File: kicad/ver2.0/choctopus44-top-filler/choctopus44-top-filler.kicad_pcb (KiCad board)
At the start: 2 copper layers, 247.4 x 118.5 mm, 90 parts, among them SW1 SW_PUSH, SW10 SW_PUSH, SW11 SW_PUSH, SW12 SW_PUSH, SW13 SW_PUSH, SW14 SW_PUSH, SW15 SW_PUSH, SW16 SW_PUSH, SW17 SW_PUSH, SW18 SW_PUSH, SW19 SW_PUSH, SW2 SW_PUSH, SW20 SW_PUSH, SW21 SW_PUSH, SW22 SW_PUSH, SW23 SW_PUSH, SW24 SW_PUSH, SW25 SW_PUSH, SW26 SW_PUSH, SW27 SW_PUSH, SW28 SW_PUSH, SW29 SW_PUSH, SW3 SW_PUSH, SW30 SW_PUSH, SW31 SW_PUSH, SW32 SW_PUSH, SW33 SW_PUSH, SW34 SW_PUSH, SW35 SW_PUSH, SW36 SW_PUSH, SW37 SW_PUSH, SW38 SW_PUSH, SW39 SW_PUSH, SW4 SW_PUSH, SW40 SW_PUSH, SW41 SW_PUSH, SW42 SW_PUSH, SW43 SW_PUSH, SW44 SW_PUSH, SW45 Rotary_Encoder_Switch, SW5 SW_PUSH, SW6 SW_PUSH, SW7 SW_PUSH, SW8 SW_PUSH, SW9 SW_PUSH

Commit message: simplify filler foam files for faster laser cutting
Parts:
- removed D37, D38, D39, D40, D41, D42, D43, D44: 1N4148W, custom-electronics:hybrid-diode-topfoam-cutout
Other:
- outline, holes or cut-outs redrawn

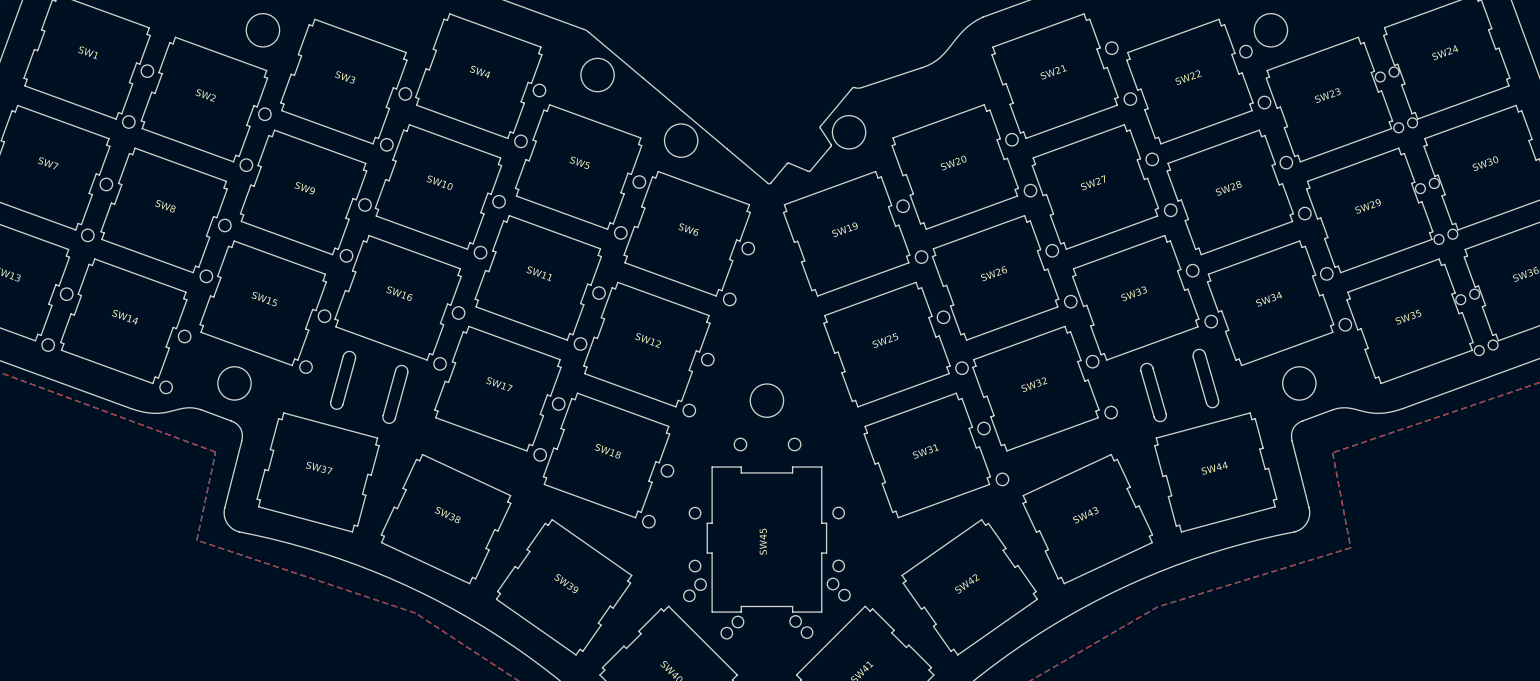
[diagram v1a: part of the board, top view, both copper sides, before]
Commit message: modify foam files to have better cutting tolerances
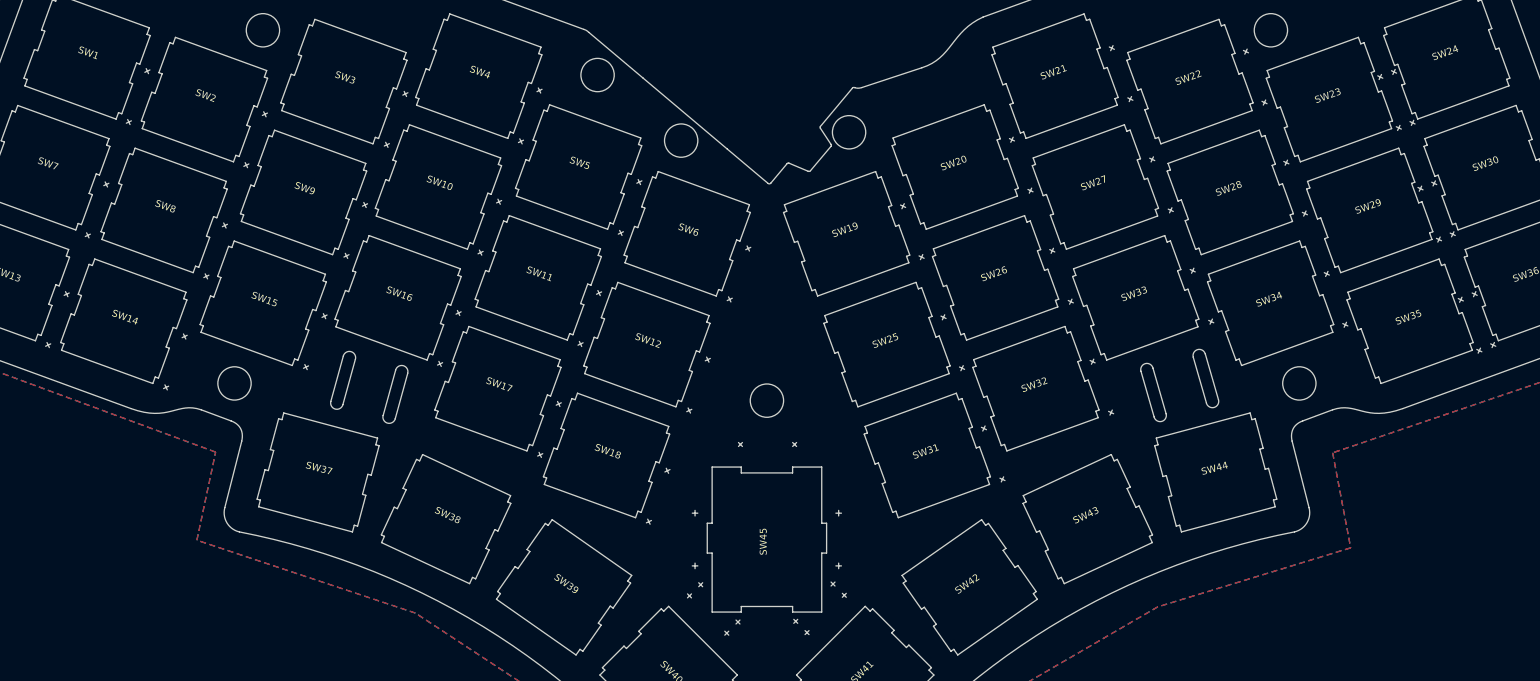
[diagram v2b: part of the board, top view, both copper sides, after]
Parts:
- added D22: 1N4148W, custom-electronics:hybrid-diode-topfoam-cutout, F.Cu at (243.8, 73.5)
- added D22: 1N4148W, custom-electronics:hybrid-diode-topfoam-cutout, F.Cu at (238.0, 57.4)
- added D22: 1N4148W, custom-electronics:hybrid-diode-topfoam-cutout, F.Cu at (249.6, 89.4)
- added D22: 1N4148W, custom-electronics:hybrid-diode-topfoam-cutout, F.Cu at (241.8, 74.2)
- added D22: 1N4148W, custom-electronics:hybrid-diode-topfoam-cutout, F.Cu at (236.0, 58.1)
- added D22: 1N4148W, custom-electronics:hybrid-diode-topfoam-cutout, F.Cu at (247.6, 90.3)
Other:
- outline, holes or cut-outs redrawn

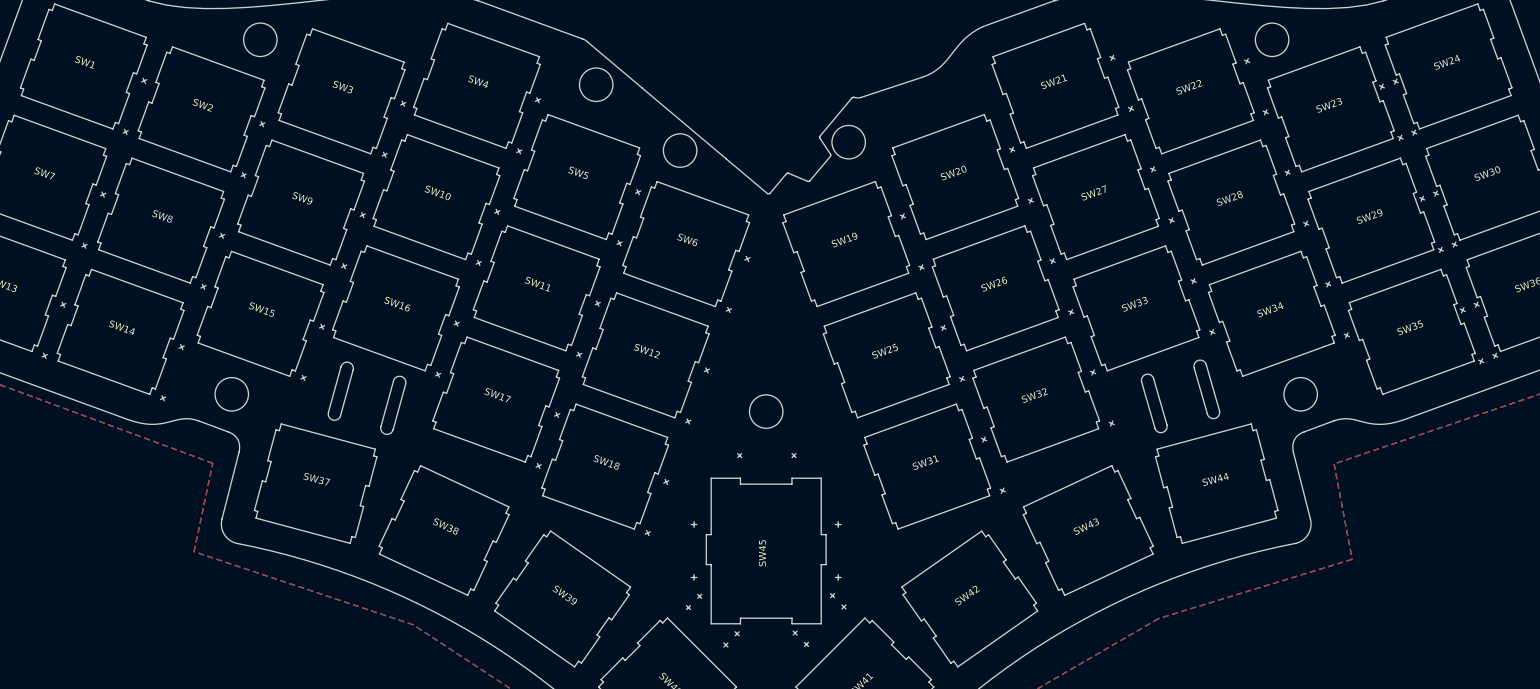
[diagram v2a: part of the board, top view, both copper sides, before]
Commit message: further optimize switch plate foams for laser cutting
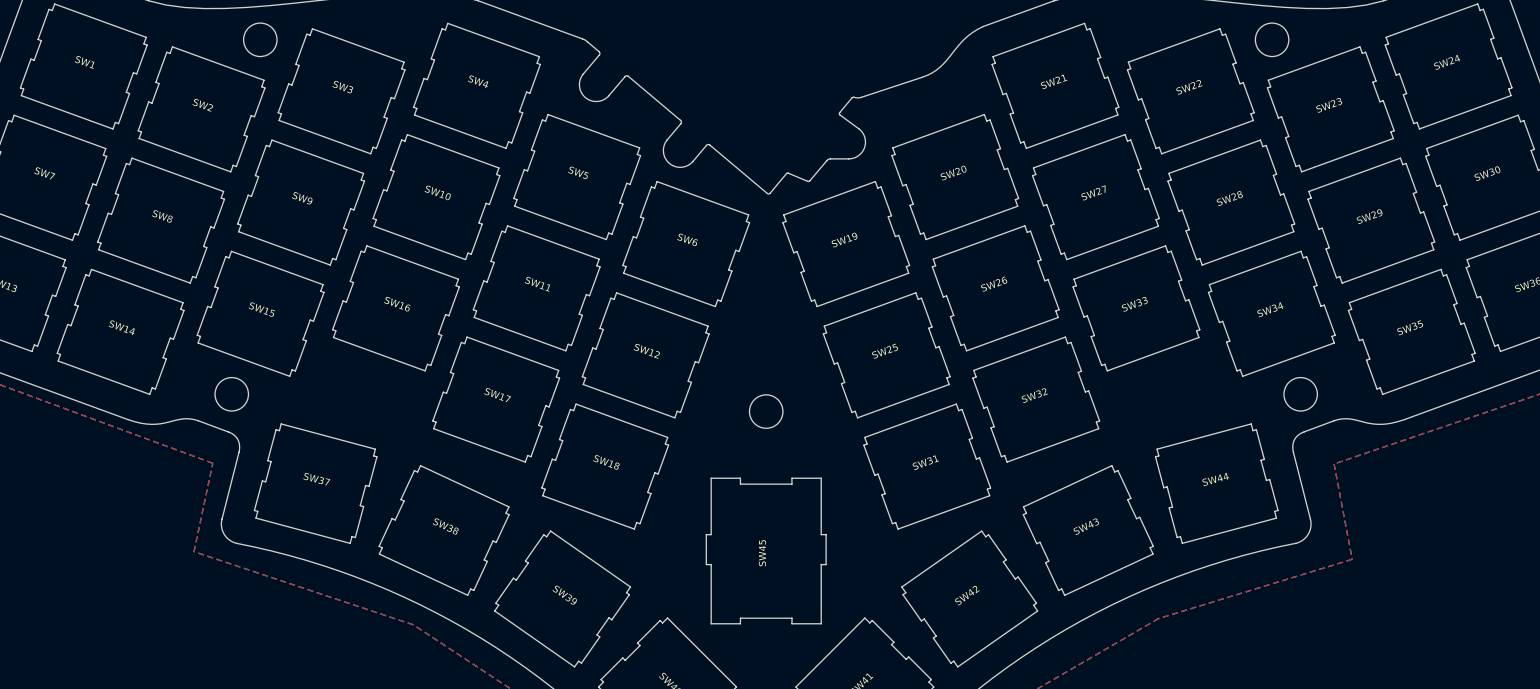
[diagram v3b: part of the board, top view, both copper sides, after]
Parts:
- removed C1, C2: C, custom-electronics:1206_hybrid-topfoam-cutout
- removed D1, D10, D11, D12, D13, D14, D15, D16, D17, D18, D19, D2, D20, D21, D22 (x7), D25, D26, D27, D28, D3, D31, D32, D33, D34, D4, D45, D5, D6, D7, D8, D9: 1N4148W, custom-electronics:hybrid-diode-topfoam-cutout
- removed R1, R2, R3, R4: R, custom-electronics:1206_hybrid-topfoam-cutout
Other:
- outline, holes or cut-outs redrawn
